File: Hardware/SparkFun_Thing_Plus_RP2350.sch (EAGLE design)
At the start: 93 parts, among them J1 THING_PLUS_LOGICAL, J3 QWIIC_RIGHT_ANGLE, J6 MICRO-SD-ATOM, Q1 100mA/20V/3.8Ω, U1 RP2350A, U10 ESD Diode, U11 APS6404L-3SQR-ZR, U2 RM2, U3 RT9080-33GJ5, U4 LM66200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

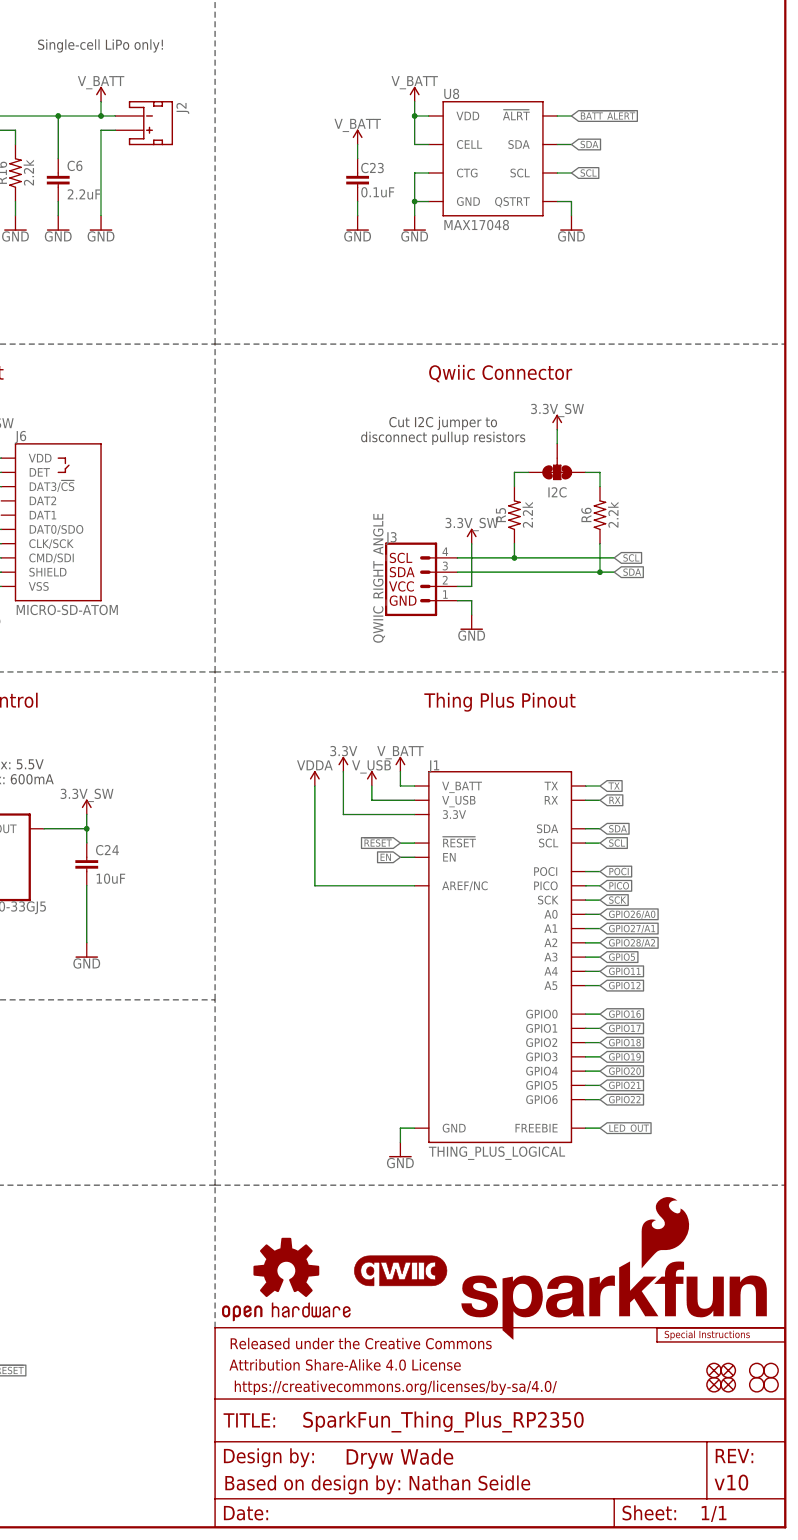
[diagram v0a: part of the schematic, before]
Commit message: Fix battery polarity
Bump version number to v11
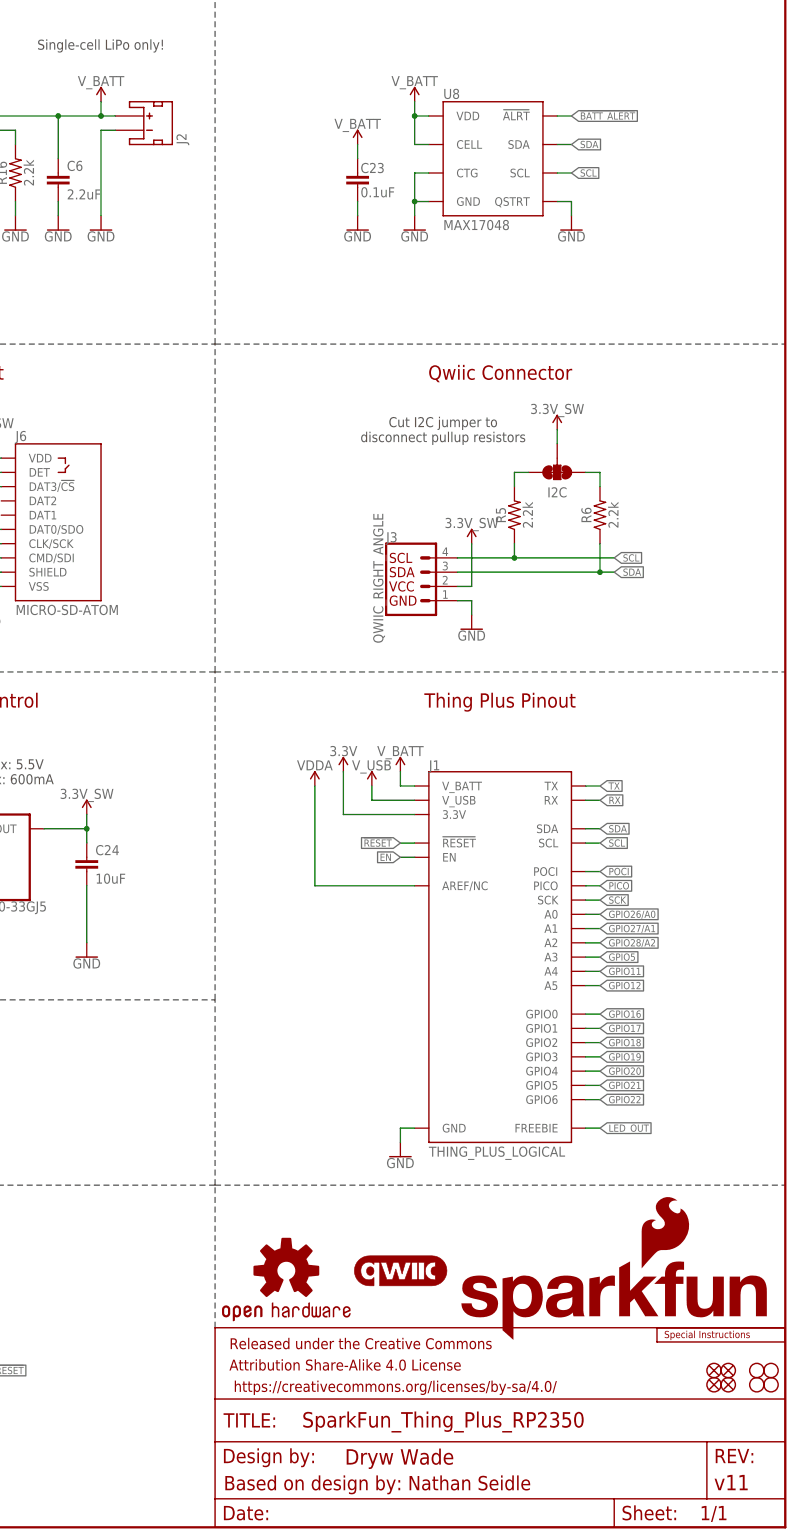
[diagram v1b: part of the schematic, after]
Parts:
- FRAME1: REV v10 -> v11
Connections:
- net GND: now also J2.-; no longer J2.+
- net V_BATT: now also J2.+; no longer J2.-
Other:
- moved on the sheet: J2
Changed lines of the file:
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@@
 <part name="FRAME1" library="SparkFun-Aesthetics" deviceset="FRAME-LEDGER" device="">
 <attribute name="DESIGNER" value="Dryw Wade"/>
-<attribute name="REV" value="v10"/>
+<attribute name="REV" value="v11"/>
 </part>
 <part name="Y1" library="SparkFun-Clocks" deviceset="CRYSTAL-12MHZ" device="" value="12MHz"/>
@@
 <attribute name="NAME" x="368.3" y="134.874" size="1.778" layer="95" font="vector"/>
 </instance>
-<instance part="J2" gate="G$1" x="317.5" y="251.46" smashed="yes" rot="R270">
-<attribute name="NAME" x="323.342" y="254" size="1.778" layer="95" rot="R270"/>
+<instance part="J2" gate="G$1" x="317.5" y="248.92" smashed="yes" rot="MR90">
+<attribute name="NAME" x="323.342" y="246.38" size="1.778" layer="95" rot="MR90"/>
 </instance>
 <instance part="J3" gate="J1" x="365.76" y="167.64" smashed="yes">
@@
 <segment>
 <pinref part="GND5" gate="1" pin="GND"/>
-<pinref part="J2" gate="G$1" pin="+"/>
 <wire x1="309.88" y1="233.68" x2="309.88" y2="248.92" width="0.1524" layer="91"/>
-<wire x1="309.88" y1="248.92" x2="312.42" y2="248.92" width="0.1524" layer="91"/>
+<pinref part="J2" gate="G$1" pin="-"/>
+<wire x1="312.42" y1="248.92" x2="309.88" y2="248.92" width="0.1524" layer="91"/>
 </segment>
 <segment>
@@
 </segment>
 <segment>
-<pinref part="J2" gate="G$1" pin="-"/>
 <pinref part="SUPPLY9" gate="G$1" pin="V_BATT"/>
-<wire x1="312.42" y1="251.46" x2="309.88" y2="251.46" width="0.1524" layer="91"/>
 <wire x1="309.88" y1="251.46" x2="309.88" y2="254" width="0.1524" layer="91"/>
 <pinref part="U6" gate="G$1" pin="VBAT"/>
 <wire x1="284.48" y1="251.46" x2="302.26" y2="251.46" width="0.1524" layer="91"/>
-<junction x="309.88" y="251.46"/>
 <pinref part="C6" gate="G$1" pin="1"/>
 <wire x1="302.26" y1="251.46" x2="309.88" y2="251.46" width="0.1524" layer="91"/>
 <wire x1="302.26" y1="243.84" x2="302.26" y2="251.46" width="0.1524" layer="91"/>
 <junction x="302.26" y="251.46"/>
-</segment>
-<segment>
+<pinref part="J2" gate="G$1" pin="+"/>
+<wire x1="312.42" y1="251.46" x2="309.88" y2="251.46" width="0.1524" layer="91"/>
+<junction x="309.88" y="251.46"/>
+</segment>
+<segment>
